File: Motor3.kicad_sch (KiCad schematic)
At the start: 15 parts, among them J603 Direction, U601 FYSETC TMC5160

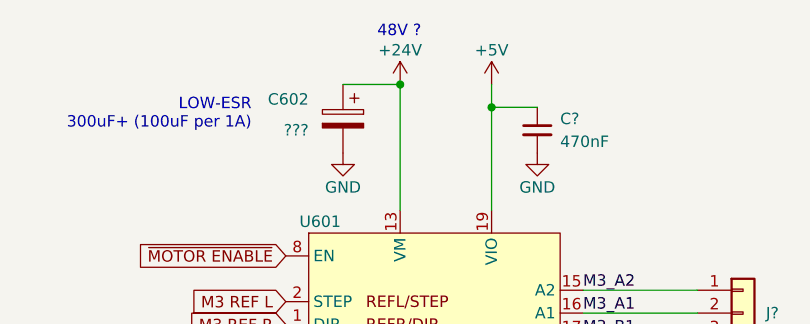
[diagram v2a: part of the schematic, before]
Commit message: More PCB placement, fix 48V for Motors
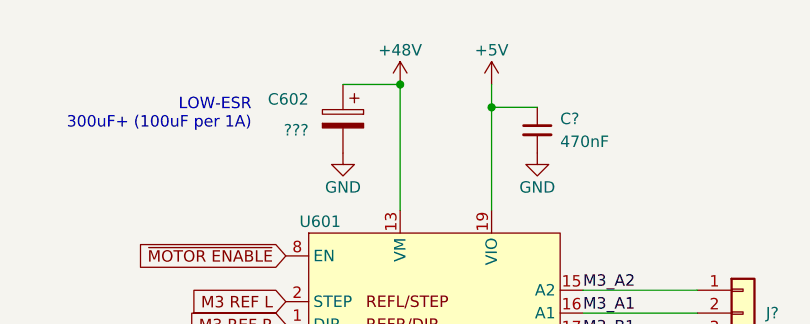
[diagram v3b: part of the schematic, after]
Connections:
- net +24V renamed +48V
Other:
- note removed: "48V ?"
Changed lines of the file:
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@@
   (junction (at 91.44 173.99) (diameter 0) (color 0 0 0 0)
   )
+  (junction (at 91.44 39.37) (diameter 0) (color 0 0 0 0)
+  )
   (junction (at 100.33 173.99) (diameter 0) (color 0 0 0 0)
   )
@@
   (junction (at 101.6 41.91) (diameter 0) (color 0 0 0 0)
   )
-  (junction (at 91.44 39.37) (diameter 0) (color 0 0 0 0)
-  )
   (wire (pts (xy 118.11 180.34) (xy 121.92 180.34))
     (stroke (width 0) (type default))
@@
   (wire (pts (xy 53.34 173.99) (xy 50.8 173.99))
     (stroke (width 0) (type default))
-  )
-  (text "48V ?" (at 88.9 34.29 0)
-    (effects (font (size 1.27 1.27)) (justify left bottom))
   )
   (text "Step Reference Output" (at 27.94 153.67 0)
@@
     )
   )
+  (symbol (lib_id "power:+48V") (at 91.44 39.37 0) (unit 1)
+    (in_bom yes) (on_board yes) (dnp no)
+    (property "Reference" "#PWR0204" (at 91.44 43.18 0)
+      (effects (font (size 1.27 1.27)) hide)
+    )
+    (property "Value" "+48V" (at 91.44 35.56 0)
+      (effects (font (size 1.27 1.27)))
+    )
+    (property "Footprint" "" (at 91.44 39.37 0)
+      (effects (font (size 1.27 1.27)) hide)
+    )
+    (property "Datasheet" "" (at 91.44 39.37 0)
+      (effects (font (size 1.27 1.27)) hide)
+    )
+    (pin "1")
+    (instances
+      (project "Can3DPrinter4Motor"
+        (path "/cb4e159a-5c17-494a-ba7f-10e700f814f1/e05e1111-b676-4692-8151-4de155805267"
+          (reference "#PWR0204") (unit 1)
+        )
+        (path "/cb4e159a-5c17-494a-ba7f-10e700f814f1"
+          (reference "#PWR0113") (unit 1)
+        )
+        (path "/cb4e159a-5c17-494a-ba7f-10e700f814f1/03ab3e80-f454-40c8-8f97-43a0b791de0b/596394bf-80ea-4be7-ad96-94dd67657b85"
+          (reference "#PWR0801") (unit 1)
+        )
+      )
+    )
+  )
   (symbol (lib_id "power:+5V") (at 121.92 168.91 0) (mirror y) (unit 1)
     (in_bom yes) (on_board yes) (dnp no)
@@
         )
       )
-    )
-  )
-  (symbol (lib_id "power:+24V") (at 91.44 39.37 0) (unit 1)
-    (in_bom yes) (on_board yes) (dnp no)
-    (property "Reference" "#PWR?" (at 91.44 43.18 0)
-      (effects (font (size 1.27 1.27)) hide)
-    )
-    (property "Value" "+24V" (at 91.44 35.56 0)
-      (effects (font (size 1.27 1.27)))
-    )
-    (property "Footprint" "" (at 91.44 39.37 0)
-      (effects (font (size 1.27 1.27)) hide)
-    )
-    (property "Datasheet" "" (at 91.44 39.37 0)
-      (effects (font (size 1.27 1.27)) hide)
-    )
-    (pin "1")
-    (instances
-      (project "Can3DPrinter4Motor"
-        (path "/cb4e159a-5c17-494a-ba7f-10e700f814f1/03ab3e80-f454-40c8-8f97-43a0b791de0b"
-          (reference "#PWR?") (unit 1)
-        )
-        (path "/cb4e159a-5c17-494a-ba7f-10e700f814f1/03ab3e80-f454-40c8-8f97-43a0b791de0b/a3514610-4e2d-47ba-84b8-39806e951746"
-          (reference "#PWR0635") (unit 1)
-        )
-        (path "/cb4e159a-5c17-494a-ba7f-10e700f814f1/03ab3e80-f454-40c8-8f97-43a0b791de0b/c731393f-82c9-42eb-b1cc-cc38a32cf9d8"
-          (reference "#PWR0705") (unit 1)
-        )
-        (path "/cb4e159a-5c17-494a-ba7f-10e700f814f1/03ab3e80-f454-40c8-8f97-43a0b791de0b/596394bf-80ea-4be7-ad96-94dd67657b85"
-          (reference "#PWR0805") (unit 1)
-        )
-        (path "/cb4e159a-5c17-494a-ba7f-10e700f814f1/03ab3e80-f454-40c8-8f97-43a0b791de0b/47aa3abf-8d06-4c45-872c-33ec1f9a6564"
-          (reference "#PWR0905") (unit 1)
-        )
-      )

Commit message: Finish wiring PCB
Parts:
- C602: footprint (none) -> Capacitor_THT:CP_Radial_D6.3mm_P2.50mm
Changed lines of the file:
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@@
     (pin "1")
     (instances
-      (project "Can3DPrinter4Motor"
+      (project "4MotorCAN"
         (path "/cb4e159a-5c17-494a-ba7f-10e700f814f1/03ab3e80-f454-40c8-8f97-43a0b791de0b"
           (reference "#PWR?") (unit 1)
@@
     (pin "2")
     (instances
-      (project "Can3DPrinter4Motor"
+      (project "4MotorCAN"
         (path "/cb4e159a-5c17-494a-ba7f-10e700f814f1/03ab3e80-f454-40c8-8f97-43a0b791de0b"
           (reference "C?") (unit 1)
@@
       (effects (font (size 1.27 1.27)) (justify left))
     )
-    (property "Footprint" "" (at 84.1248 46.99 0)
+    (property "Footprint" "Capacitor_THT:CP_Radial_D6.3mm_P2.50mm" (at 84.1248 46.99 0)
       (effects (font (size 1.27 1.27)) hide)
     )
@@
       (effects (font (size 1.27 1.27)) hide)
     )
-    (pin "1")
-    (pin "2")
-    (instances
-      (project "Can3DPrinter4Motor"
+    (property "LCSC" "" (at 85.09 43.18 0)
+      (effects (font (size 1.27 1.27)) hide)
+    )
+    (pin "1")
+    (pin "2")
+    (instances
+      (project "4MotorCAN"
         (path "/cb4e159a-5c17-494a-ba7f-10e700f814f1/03ab3e80-f454-40c8-8f97-43a0b791de0b/a3514610-4e2d-47ba-84b8-39806e951746"
           (reference "C602") (unit 1)
@@
     (pin "2")
     (instances
-      (project "Can3DPrinter4Motor"
+      (project "4MotorCAN"
         (path "/cb4e159a-5c17-494a-ba7f-10e700f814f1/03ab3e80-f454-40c8-8f97-43a0b791de0b"
           (reference "R?") (unit 1)
@@
     (pin "4")
     (instances
-      (project "Can3DPrinter4Motor"
+      (project "4MotorCAN"
         (path "/cb4e159a-5c17-494a-ba7f-10e700f814f1/03ab3e80-f454-40c8-8f97-43a0b791de0b/a3514610-4e2d-47ba-84b8-39806e951746"
           (reference "J603") (unit 1)
@@
     (pin "1")
     (instances
-      (project "Can3DPrinter4Motor"
+      (project "4MotorCAN"
         (path "/cb4e159a-5c17-494a-ba7f-10e700f814f1/03ab3e80-f454-40c8-8f97-43a0b791de0b"
           (reference "#PWR?") (unit 1)
@@
     (pin "1")
     (instances
-      (project "Can3DPrinter4Motor"
+      (project "4MotorCAN"
         (path "/cb4e159a-5c17-494a-ba7f-10e700f814f1/03ab3e80-f454-40c8-8f97-43a0b791de0b/a3514610-4e2d-47ba-84b8-39806e951746"
           (reference "#PWR0619") (unit 1)
@@
     (pin "1")
     (instances
-      (project "Can3DPrinter4Motor"
+      (project "4MotorCAN"
         (path "/cb4e159a-5c17-494a-ba7f-10e700f814f1/03ab3e80-f454-40c8-8f97-43a0b791de0b"
           (reference "#PWR?") (unit 1)
@@
     (pin "1")
     (instances
-      (project "Can3DPrinter4Motor"
+      (project "4MotorCAN"
         (path "/cb4e159a-5c17-494a-ba7f-10e700f814f1/e05e1111-b676-4692-8151-4de155805267"
           (reference "#PWR0204") (unit 1)
@@
     (pin "1")
     (instances
-      (project "Can3DPrinter4Motor"
+      (project "4MotorCAN"
         (path "/cb4e159a-5c17-494a-ba7f-10e700f814f1/03ab3e80-f454-40c8-8f97-43a0b791de0b/a3514610-4e2d-47ba-84b8-39806e951746"
           (reference "#PWR0623") (unit 1)
@@
     (pin "2")
     (instances
-      (project "Can3DPrinter4Motor"
+      (project "4MotorCAN"
         (path "/cb4e159a-5c17-494a-ba7f-10e700f814f1/03ab3e80-f454-40c8-8f97-43a0b791de0b"
           (reference "C?") (unit 1)
@@
     (pin "1")
     (instances
-      (project "Can3DPrinter4Motor"
+      (project "4MotorCAN"
         (path "/cb4e159a-5c17-494a-ba7f-10e700f814f1/03ab3e80-f454-40c8-8f97-43a0b791de0b"
           (reference "#PWR?") (unit 1)
@@
         )
       )
-      (project "Can3DPrinter4Motor"
+      (project "4MotorCAN"
         (path "/cb4e159a-5c17-494a-ba7f-10e700f814f1"
           (reference "D104") (unit 1)
@@
     (pin "2")
     (instances
-      (project "Can3DPrinter4Motor"
+      (project "4MotorCAN"
         (path "/cb4e159a-5c17-494a-ba7f-10e700f814f1/03ab3e80-f454-40c8-8f97-43a0b791de0b"
           (reference "R?") (unit 1)
@@
     (pin "1")
     (instances
-      (project "Can3DPrinter4Motor"
+      (project "4MotorCAN"
         (path "/cb4e159a-5c17-494a-ba7f-10e700f814f1/03ab3e80-f454-40c8-8f97-43a0b791de0b"
           (reference "#PWR?") (unit 1)
@@
     (pin "2")
     (instances
-      (project "Can3DPrinter4Motor"
+      (project "4MotorCAN"
         (path "/cb4e159a-5c17-494a-ba7f-10e700f814f1/03ab3e80-f454-40c8-8f97-43a0b791de0b"
           (reference "C?") (unit 1)
@@
     (pin "1")
     (instances
-      (project "Can3DPrinter4Motor"
+      (project "4MotorCAN"
         (path "/cb4e159a-5c17-494a-ba7f-10e700f814f1/03ab3e80-f454-40c8-8f97-43a0b791de0b"
           (reference "#PWR?") (unit 1)
@@
     (pin "1")
     (instances
-      (project "Can3DPrinter4Motor"
+      (project "4MotorCAN"
         (path "/cb4e159a-5c17-494a-ba7f-10e700f814f1/03ab3e80-f454-40c8-8f97-43a0b791de0b"
           (reference "#PWR?") (unit 1)
@@
     (pin "1")
     (instances
-      (project "Can3DPrinter4Motor"
+      (project "4MotorCAN"
         (path "/cb4e159a-5c17-494a-ba7f-10e700f814f1/03ab3e80-f454-40c8-8f97-43a0b791de0b/a3514610-4e2d-47ba-84b8-39806e951746"
           (reference "#PWR0634") (unit 1)
@@
     (pin "1")
     (instances
-      (project "Can3DPrinter4Motor"
+      (project "4MotorCAN"
         (path "/cb4e159a-5c17-494a-ba7f-10e700f814f1/03ab3e80-f454-40c8-8f97-43a0b791de0b/a3514610-4e2d-47ba-84b8-39806e951746"
           (reference "#PWR0626") (unit 1)
@@
     (pin "1")
     (instances
-      (project "Can3DPrinter4Motor"
+      (project "4MotorCAN"
         (path "/cb4e159a-5c17-494a-ba7f-10e700f814f1/03ab3e80-f454-40c8-8f97-43a0b791de0b"
           (reference "#PWR?") (unit 1)
@@
     (pin "5")
     (instances
-      (project "Can3DPrinter4Motor"
+      (project "4MotorCAN"
         (path "/cb4e159a-5c17-494a-ba7f-10e700f814f1/03ab3e80-f454-40c8-8f97-43a0b791de0b"
           (reference "J?") (unit 1)
@@
     (pin "2")
     (instances
-      (project "Can3DPrinter4Motor"
+      (project "4MotorCAN"
         (path "/cb4e159a-5c17-494a-ba7f-10e700f814f1/03ab3e80-f454-40c8-8f97-43a0b791de0b"
           (reference "R?") (unit 1)
@@
         )
       )
-      (project "Can3DPrinter4Motor"
+      (project "4MotorCAN"
         (path "/cb4e159a-5c17-494a-ba7f-10e700f814f1"
           (reference "R104") (unit 1)
@@
     (pin "4")
     (instances
-      (project "Can3DPrinter4Motor"
+      (project "4MotorCAN"
         (path "/cb4e159a-5c17-494a-ba7f-10e700f814f1/03ab3e80-f454-40c8-8f97-43a0b791de0b"
           (reference "J?") (unit 1)
@@
     (pin "1")
     (instances
-      (project "Can3DPrinter4Motor"
+      (project "4MotorCAN"
         (path "/cb4e159a-5c17-494a-ba7f-10e700f814f1/03ab3e80-f454-40c8-8f97-43a0b791de0b/a3514610-4e2d-47ba-84b8-39806e951746"
           (reference "#PWR0601") (unit 1)
@@
     (pin "2")
     (instances
-      (project "Can3DPrinter4Motor"
+      (project "4MotorCAN"
         (path "/cb4e159a-5c17-494a-ba7f-10e700f814f1/03ab3e80-f454-40c8-8f97-43a0b791de0b"
           (reference "R?") (unit 1)
@@
     (pin "1")
     (instances
-      (project "Can3DPrinter4Motor"
+      (project "4MotorCAN"
         (path "/cb4e159a-5c17-494a-ba7f-10e700f814f1/03ab3e80-f454-40c8-8f97-43a0b791de0b/a3514610-4e2d-47ba-84b8-39806e951746"
           (reference "#PWR0618") (unit 1)
@@
     (pin "1")
     (instances
-      (project "Can3DPrinter4Motor"
+      (project "4MotorCAN"
         (path "/cb4e159a-5c17-494a-ba7f-10e700f814f1/03ab3e80-f454-40c8-8f97-43a0b791de0b"
           (reference "#PWR?") (unit 1)
@@
     (pin "2")
     (instances
-      (project "Can3DPrinter4Motor"
+      (project "4MotorCAN"
         (path "/cb4e159a-5c17-494a-ba7f-10e700f814f1/03ab3e80-f454-40c8-8f97-43a0b791de0b"
           (reference "R?") (unit 1)
@@
     (pin "9")
     (instances
-      (project "Can3DPrinter4Motor"
+      (project "4MotorCAN"
         (path "/cb4e159a-5c17-494a-ba7f-10e700f814f1/03ab3e80-f454-40c8-8f97-43a0b791de0b/a3514610-4e2d-47ba-84b8-39806e951746"
           (reference "U601") (unit 1)

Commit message: Finish PCB, documentation
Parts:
- C? (x2), J603, R? (x5): now left out of the parts list
- D?: now in the parts list
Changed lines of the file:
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@@
   )
   (symbol (lib_id "Device:R_Small") (at 121.92 171.45 180) (unit 1)
-    (in_bom yes) (on_board yes) (dnp yes)
+    (in_bom no) (on_board yes) (dnp yes)
     (property "Reference" "R?" (at 120.65 170.18 0)
       (effects (font (size 1.27 1.27)) (justify left))
@@
   )
   (symbol (lib_id "Connector_Generic:Conn_02x02_Odd_Even") (at 110.49 180.34 0) (mirror x) (unit 1)
-    (in_bom yes) (on_board yes) (dnp yes)
+    (in_bom no) (on_board yes) (dnp yes)
     (property "Reference" "J603" (at 111.76 175.26 0)
       (effects (font (size 1.27 1.27)))
@@
   )
   (symbol (lib_id "Device:C_Small") (at 130.81 176.53 0) (unit 1)
-    (in_bom yes) (on_board yes) (dnp yes)
+    (in_bom no) (on_board yes) (dnp yes)
     (property "Reference" "C?" (at 133.35 175.2663 0)
       (effects (font (size 1.27 1.27)) (justify left))
@@
   )
   (symbol (lib_id "Device:LED") (at 39.37 173.99 0) (mirror x) (unit 1)
-    (in_bom no) (on_board yes) (dnp no)
+    (in_bom yes) (on_board yes) (dnp no)
     (property "Reference" "D?" (at 38.1 170.18 0)
       (effects (font (size 1.27 1.27)))
@@
   )
   (symbol (lib_id "Device:R_Small") (at 100.33 171.45 0) (mirror x) (unit 1)
-    (in_bom yes) (on_board yes) (dnp yes)
+    (in_bom no) (on_board yes) (dnp yes)
     (property "Reference" "R?" (at 101.6 170.18 0)
       (effects (font (size 1.27 1.27)) (justify left))
@@
   )
   (symbol (lib_id "Device:C_Small") (at 91.44 176.53 0) (mirror y) (unit 1)
-    (in_bom yes) (on_board yes) (dnp yes)
+    (in_bom no) (on_board yes) (dnp yes)
     (property "Reference" "C?" (at 88.9 175.2663 0)
       (effects (font (size 1.27 1.27)) (justify left))
@@
   )
   (symbol (lib_id "Device:R_Small") (at 127 173.99 270) (mirror x) (unit 1)
-    (in_bom yes) (on_board yes) (dnp yes)
+    (in_bom no) (on_board yes) (dnp yes)
     (property "Reference" "R?" (at 127 171.45 90)
       (effects (font (size 1.27 1.27)))
@@
   )
   (symbol (lib_id "Device:R_Small") (at 43.18 163.83 90) (unit 1)
-    (in_bom yes) (on_board yes) (dnp yes)
+    (in_bom no) (on_board yes) (dnp yes)
     (property "Reference" "R?" (at 43.18 161.29 90)
       (effects (font (size 1.27 1.27)))
@@
   )
   (symbol (lib_id "Device:R_Small") (at 95.25 173.99 90) (unit 1)
-    (in_bom yes) (on_board yes) (dnp yes)
+    (in_bom no) (on_board yes) (dnp yes)
     (property "Reference" "R?" (at 95.25 171.45 90)
       (effects (font (size 1.27 1.27)))
